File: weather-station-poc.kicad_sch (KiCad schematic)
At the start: 0 parts

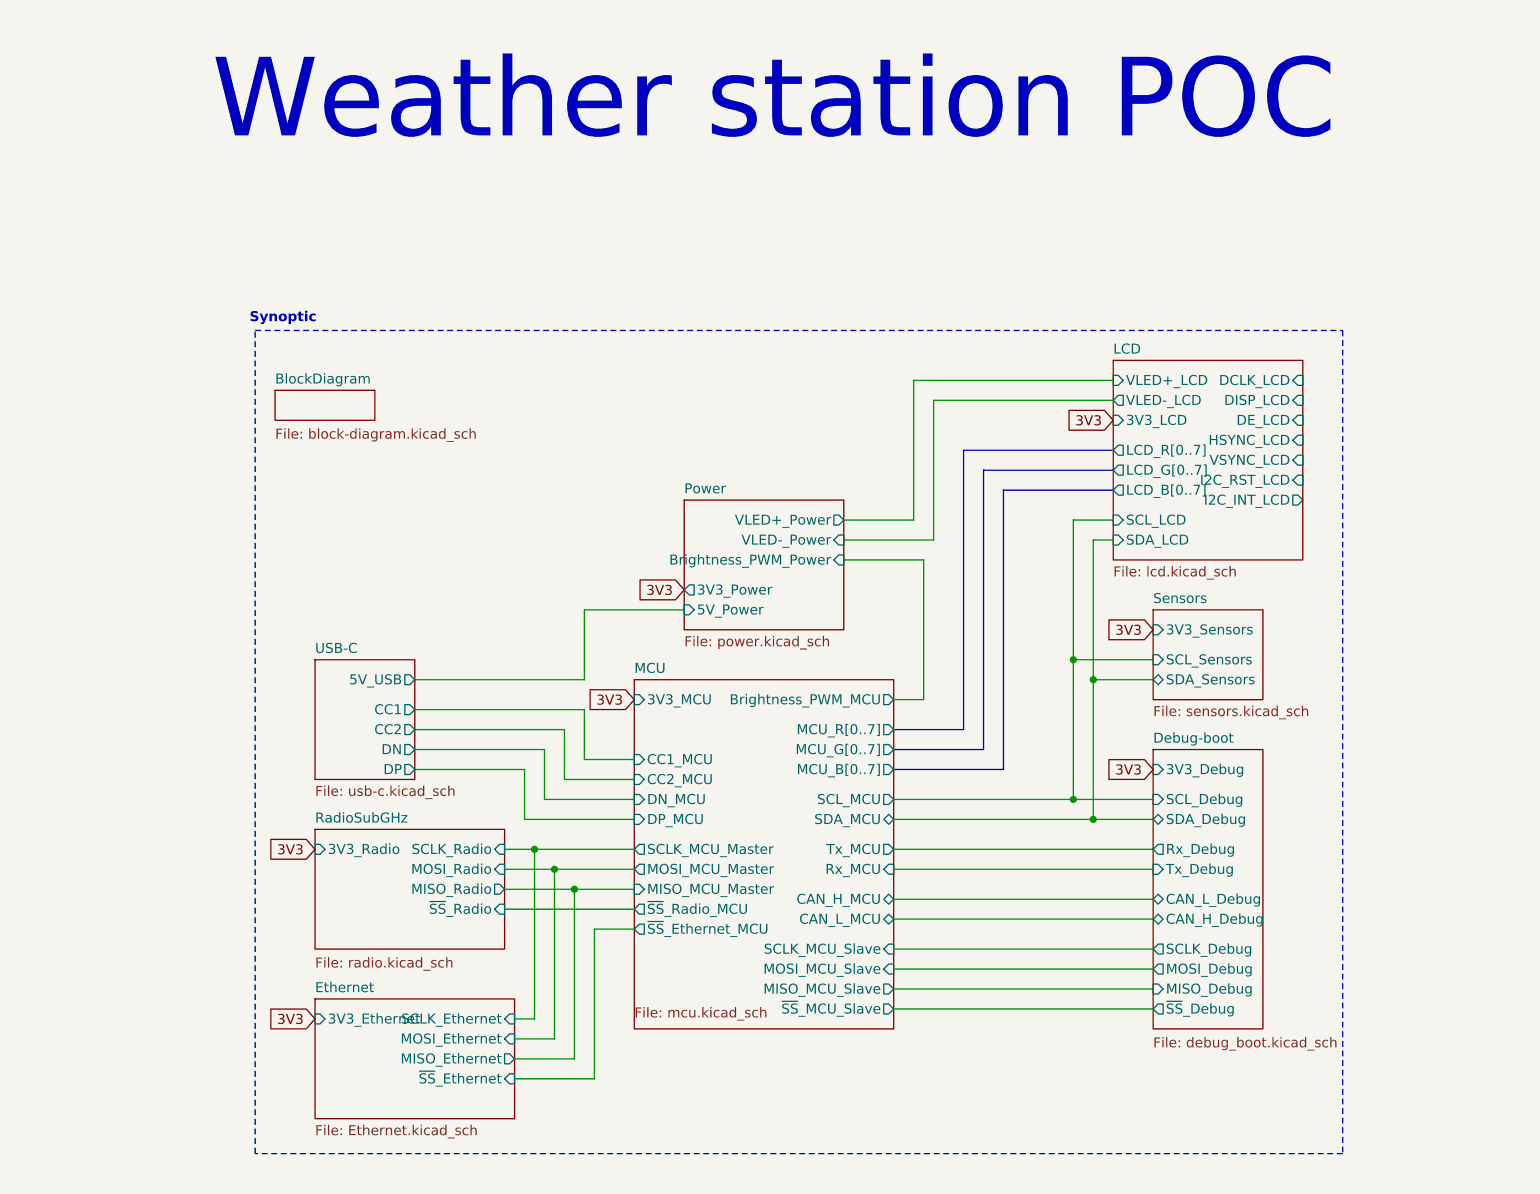
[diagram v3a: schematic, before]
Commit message: Add LCD signals to MCU and LCD folios
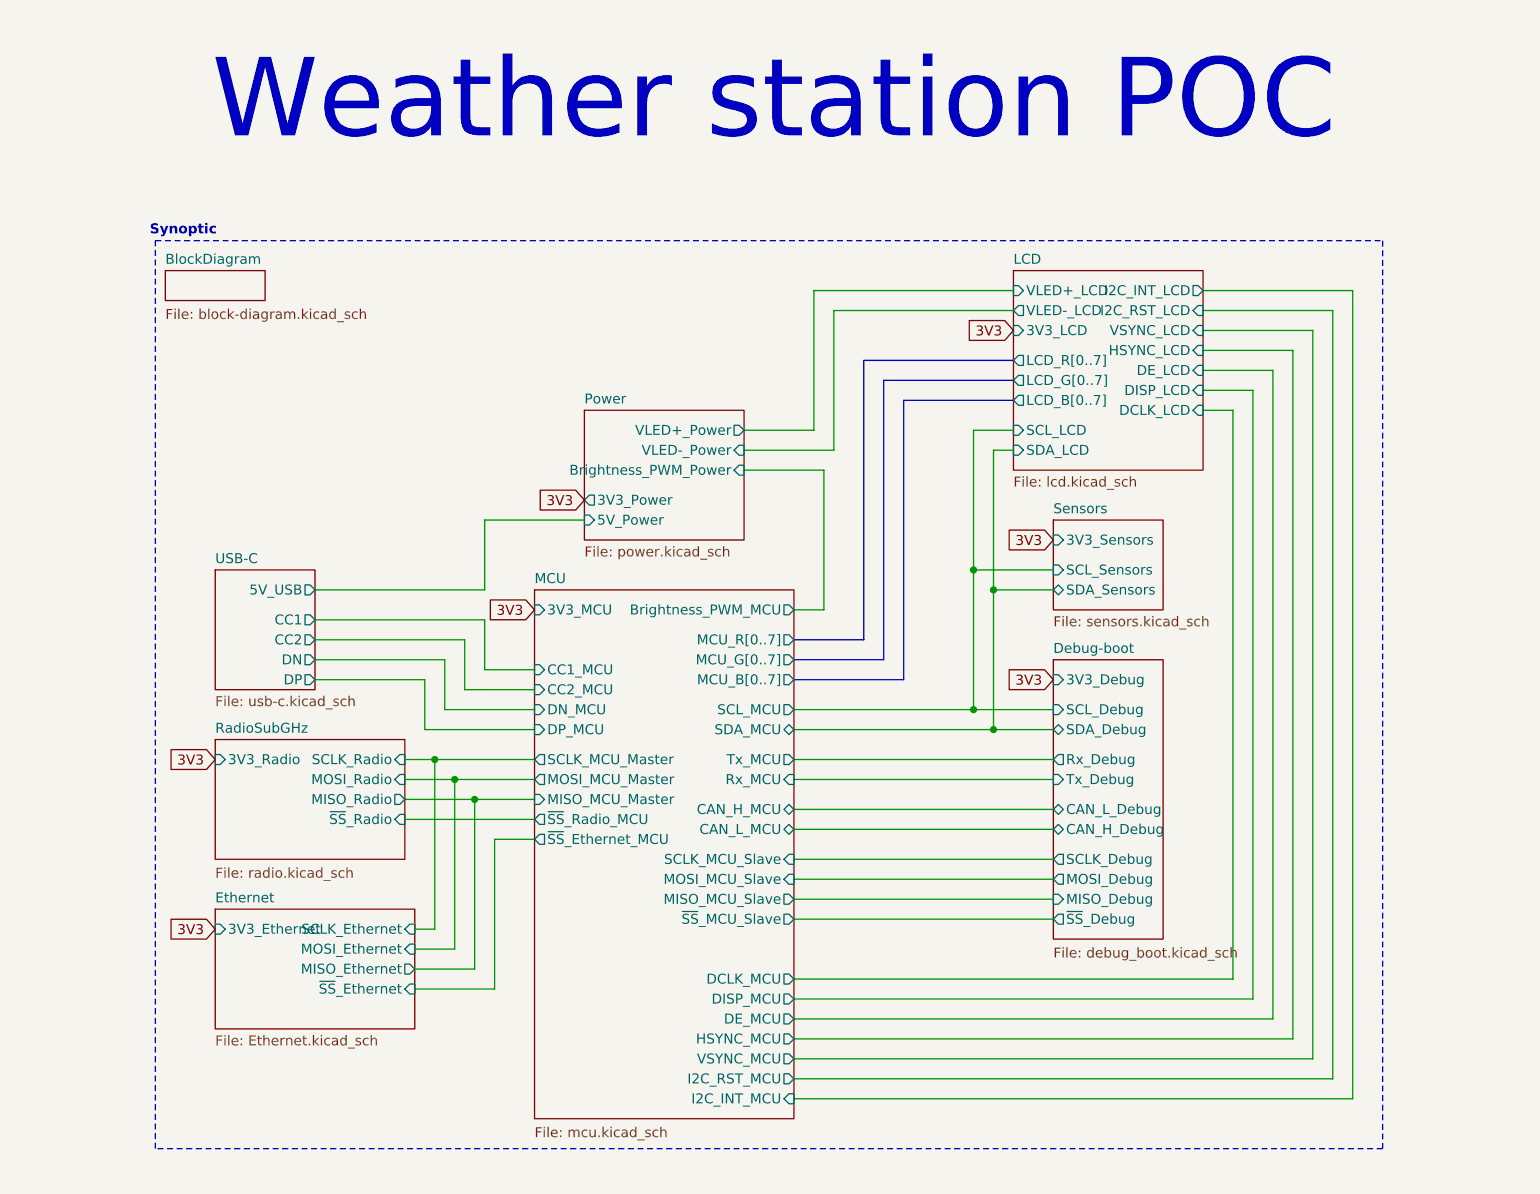
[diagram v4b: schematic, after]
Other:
- sheet MCU ports: added DCLK_MCU, DE_MCU, DISP_MCU, HSYNC_MCU, I2C_INT_MCU, I2C_RST_MCU, VSYNC_MCU; removed none

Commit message: Add SWG ARM/JTAG connector 10 pins
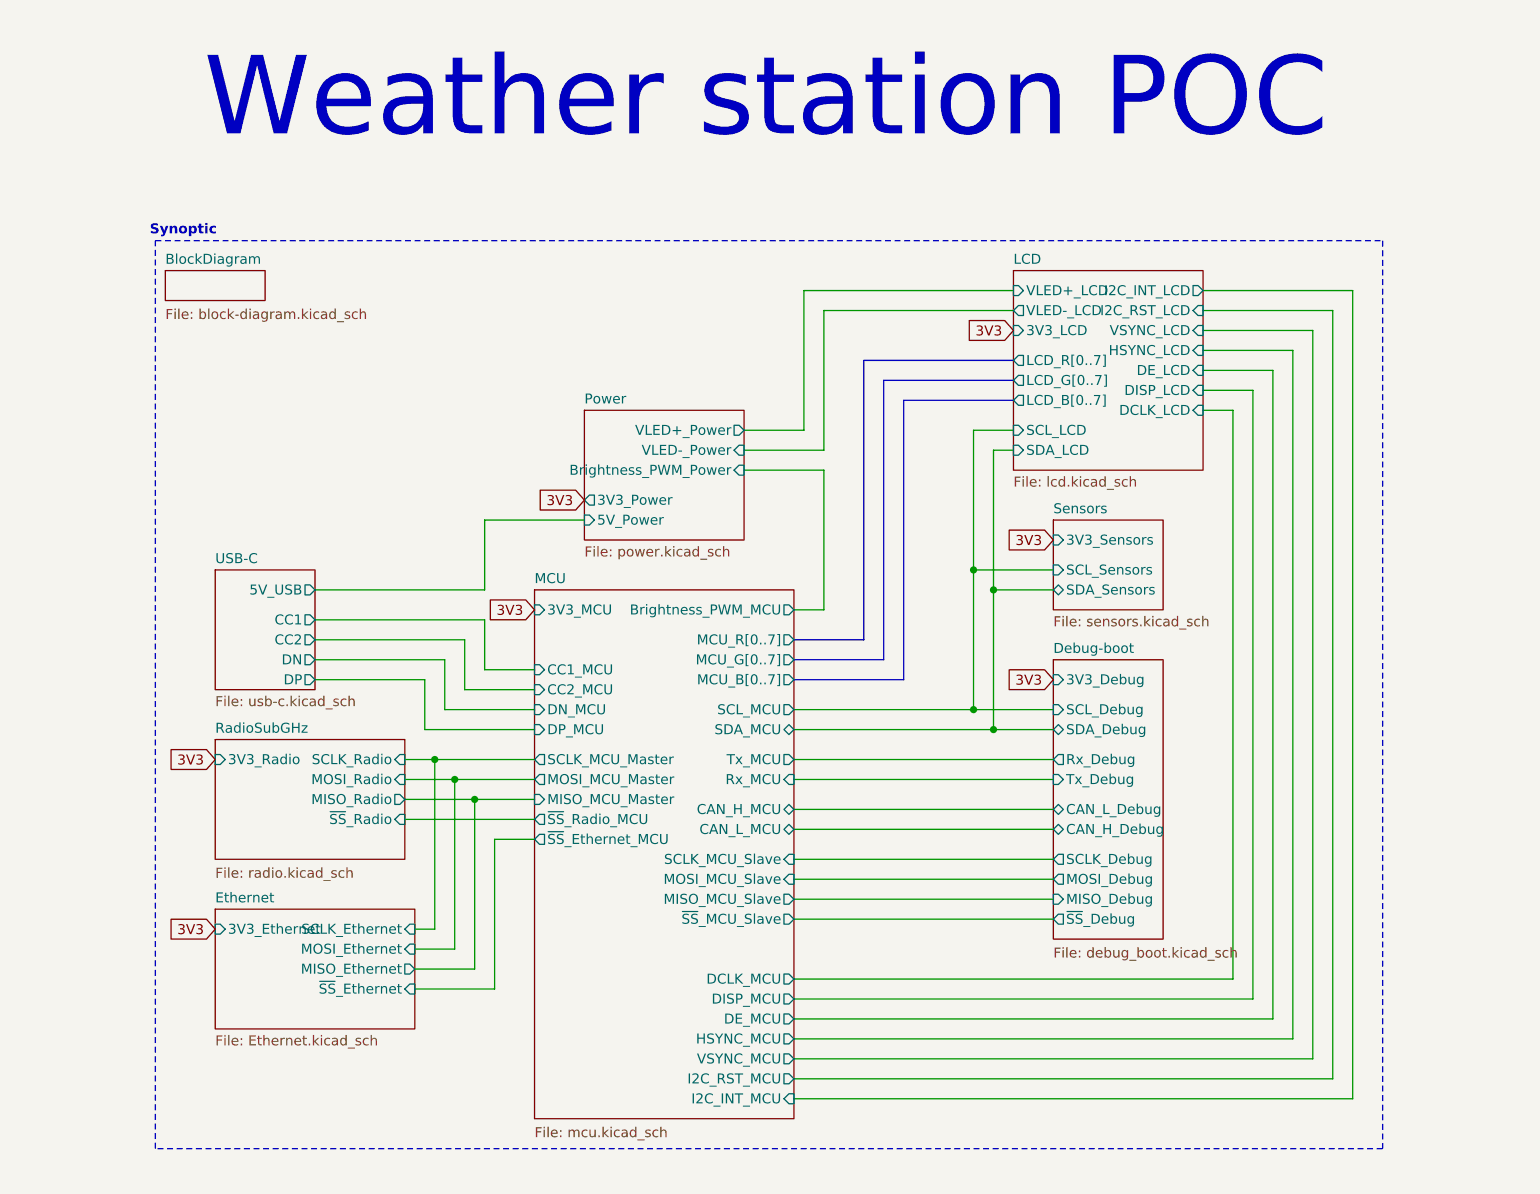
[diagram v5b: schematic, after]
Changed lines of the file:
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@@
 	(text "Weather station POC"
 		(exclude_from_sim no)
-		(at 149.86 24.13 0)
+		(at 148.844 23.876 0)
 		(effects
 			(font
@@
 	(wire
 		(pts
-			(xy 154.94 66.04) (xy 154.94 48.26)
+			(xy 153.67 66.04) (xy 153.67 48.26)
 		)
 		(stroke
@@
 	(wire
 		(pts
-			(xy 157.48 68.58) (xy 157.48 50.8)
+			(xy 156.21 68.58) (xy 156.21 50.8)
 		)
 		(stroke
@@
 	(wire
 		(pts
-			(xy 154.94 48.26) (xy 180.34 48.26)
+			(xy 153.67 48.26) (xy 180.34 48.26)
 		)
 		(stroke
@@
 	(wire
 		(pts
-			(xy 146.05 66.04) (xy 154.94 66.04)
+			(xy 146.05 66.04) (xy 153.67 66.04)
 		)
 		(stroke
@@
 	(wire
 		(pts
-			(xy 157.48 50.8) (xy 180.34 50.8)
+			(xy 156.21 50.8) (xy 180.34 50.8)
 		)
 		(stroke
@@
 	(wire
 		(pts
-			(xy 146.05 68.58) (xy 157.48 68.58)
-		)
-		(stroke
+			(xy 146.05 68.58) (xy 156.21 68.58)
+		)
+		(stroke

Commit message: Add debug connectors
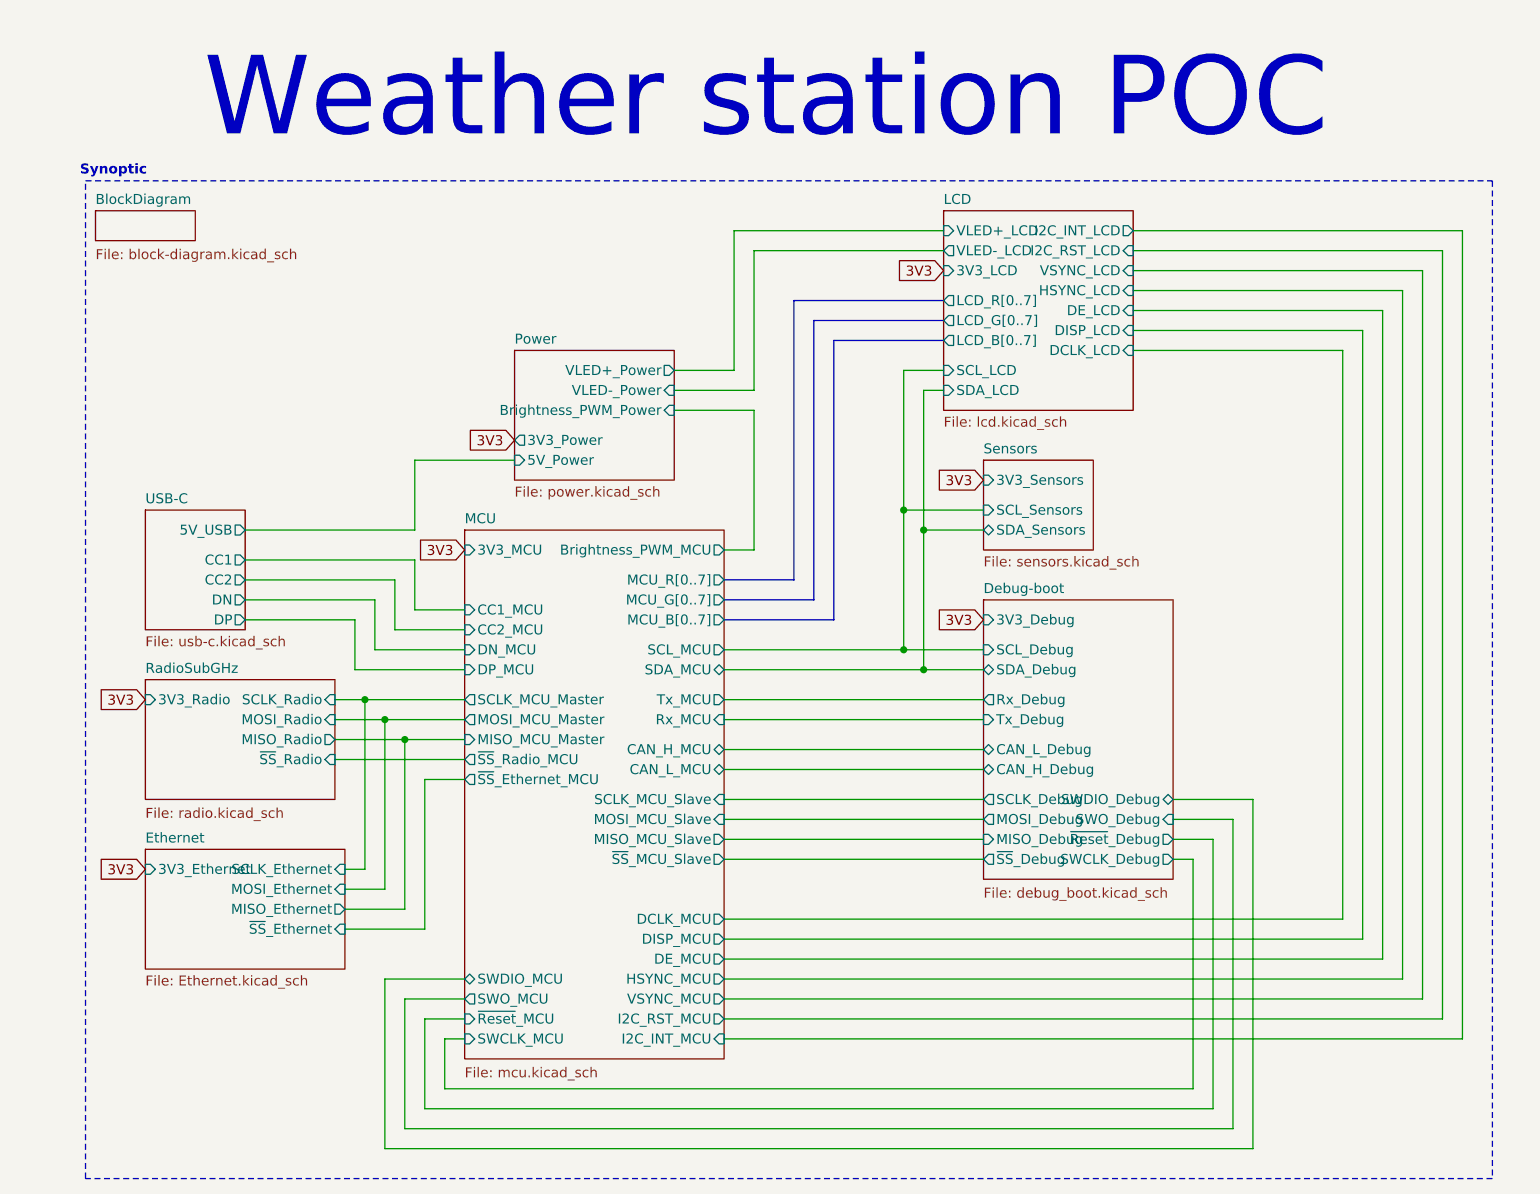
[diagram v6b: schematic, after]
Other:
- sheet Debug-boot ports: added SWCLK_Debug, SWDIO_Debug, SWO_Debug, ~{Reset}_Debug; removed none
- sheet MCU ports: added SWCLK_MCU, SWDIO_MCU, SWO_MCU, ~{Reset}_MCU; removed none

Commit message: Assign MCU pins
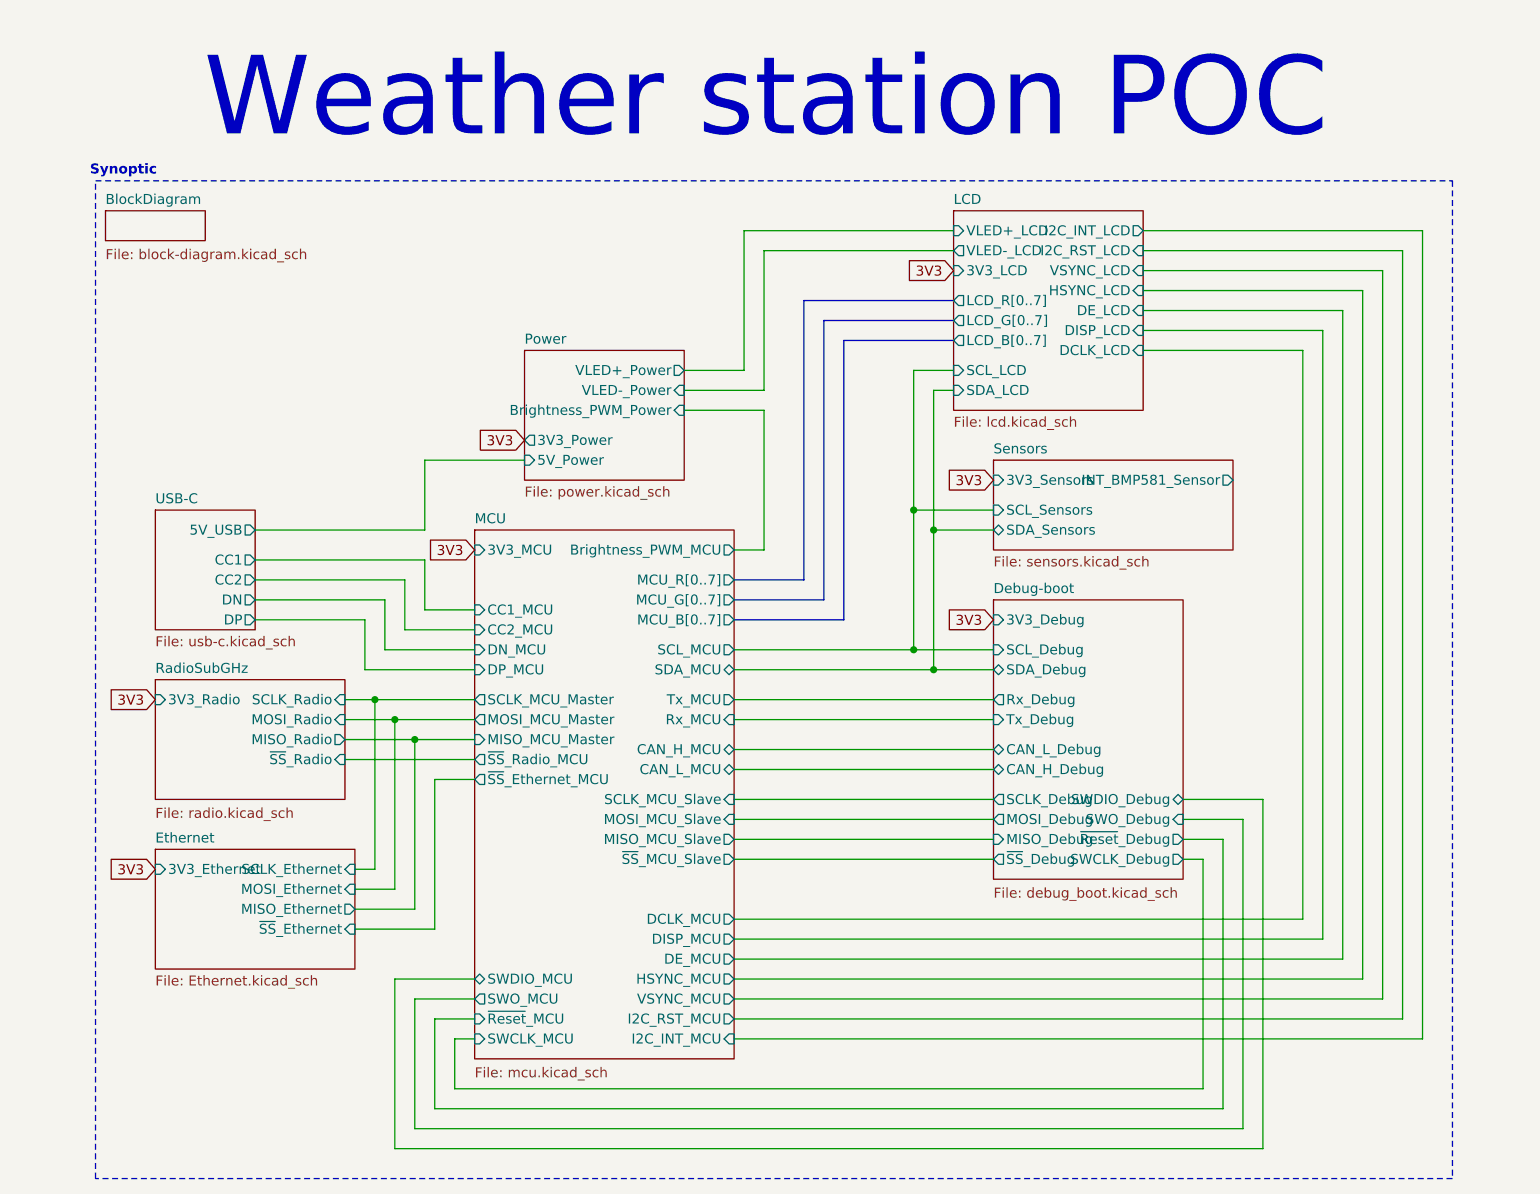
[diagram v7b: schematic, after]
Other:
- sheet Sensors ports: added INT_BMP581_Sensor; removed none

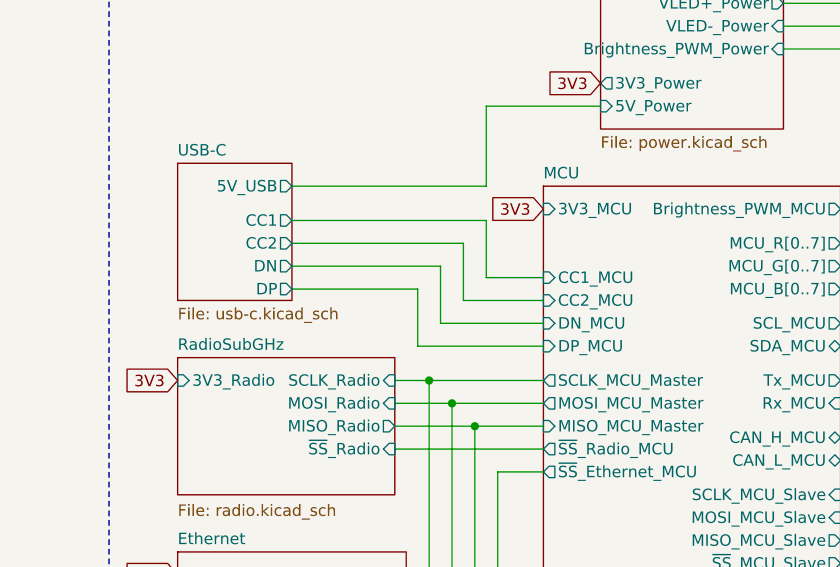
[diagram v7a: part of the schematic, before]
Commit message: Connect all pins to MCU
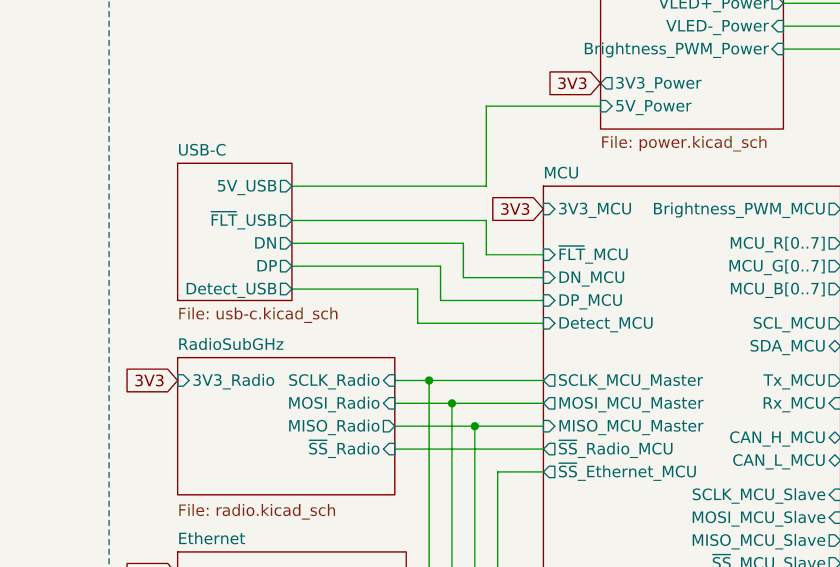
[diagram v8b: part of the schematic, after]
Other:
- sheet MCU ports: added Detect_MCU, ~{FLT}_MCU; removed CC1_MCU, CC2_MCU
- sheet USB-C ports: added Detect_USB, ~{FLT}_USB; removed CC1, CC2
